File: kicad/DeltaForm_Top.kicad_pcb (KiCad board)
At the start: 2 copper layers, 85.4 x 128.6 mm, 21 parts

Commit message: added MCU
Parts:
- moved SPMP10 270.0 mm to (466.4, 132.9)
- moved SPMP11 270.0 mm to (485.4, 132.9)
- moved SPMP13 270.0 mm to (466.4, 151.9)
- moved SPMP14 270.0 mm to (485.4, 151.9)
- moved SPMP16 270.0 mm to (466.4, 171.0)
- moved SPMP17 270.0 mm to (485.4, 171.0)
- moved SPMP18 270.0 mm to (485.4, 190.0)
- moved SPMP3 270.0 mm to (466.4, 90.0)
- moved SPMP4 270.0 mm to (466.4, 113.8)
- moved SPMP5 270.0 mm to (485.4, 90.0)
- moved SPMP6 270.0 mm to (485.4, 113.8)
- moved SPMP1 270.0 mm to (447.3, 90.0)
- moved SPMP12 270.0 mm to (447.3, 151.9)
- moved SPMP15 270.0 mm to (447.3, 171.0)
- moved SPMP19 270.0 mm to (504.5, 142.4)
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
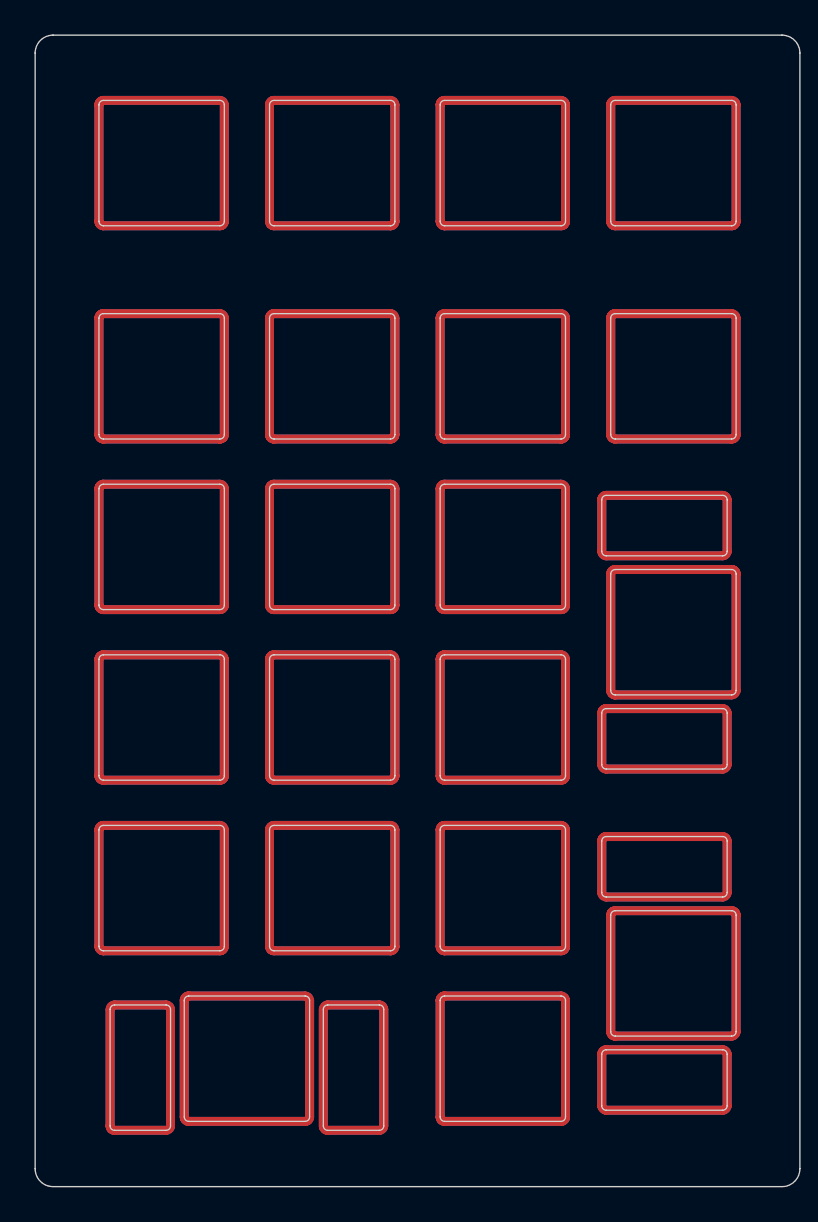
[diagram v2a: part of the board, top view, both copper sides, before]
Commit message: screw holes
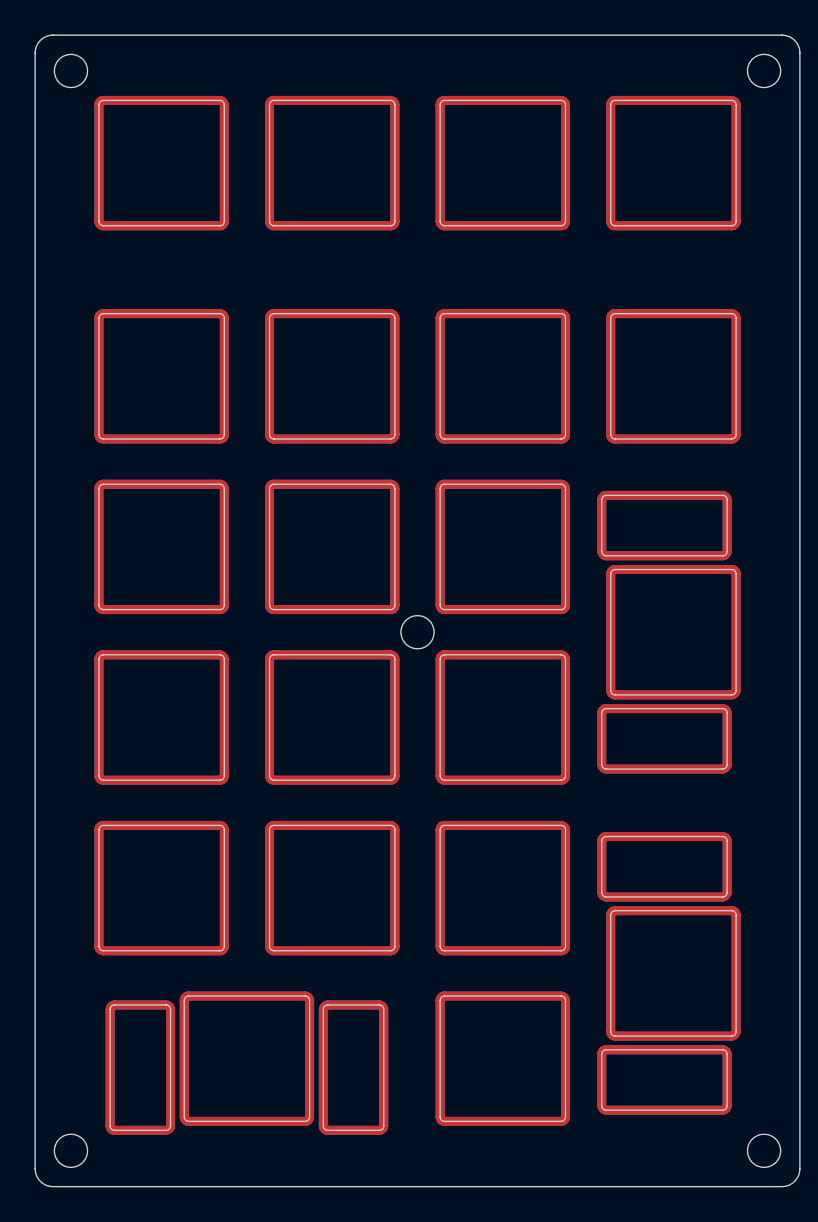
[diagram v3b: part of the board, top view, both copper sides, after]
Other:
- outline, holes or cut-outs redrawn
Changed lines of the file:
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@@
     (title "DeltaForm_Top")
     (date "2025-07-03")
-    (rev "0.3.4")
+    (rev "0.3.5")
     (company "Allen Choi")
   )
@@
 (gr_arc (start 516.575 204.3) (mid 517.9892136000001 203.71421360000002) (end 518.575 202.3) (layer Edge.Cuts) (stroke (width 0.15) (type default)))
 (gr_arc (start 433.17500000000007 202.3) (mid 433.7607864000001 203.71421360000002) (end 435.17500000000007 204.3) (layer Edge.Cuts) (stroke (width 0.15) (type default)))
+(gr_circle (center 437.17500000000007 79.7125) (end 439.0250000000001 79.7125) (layer Edge.Cuts) (stroke (width 0.15) (type default)) (fill none))
+(gr_circle (center 514.575 79.7125) (end 516.4250000000001 79.7125) (layer Edge.Cuts) (stroke (width 0.15) (type default)) (fill none))
+(gr_circle (center 514.575 200.30000000000004) (end 516.4250000000001 200.30000000000004) (layer Edge.Cuts) (stroke (width 0.15) (type default)) (fill none))
+(gr_circle (center 437.17500000000007 200.30000000000004) (end 439.0250000000001 200.30000000000004) (layer Edge.Cuts) (stroke (width 0.15) (type default)) (fill none))
+(gr_circle (center 475.87500000000006 142.38750000000002) (end 477.7250000000001 142.38750000000002) (layer Edge.Cuts) (stroke (width 0.15) (type default)) (fill none))
 )

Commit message: pogo pin - ergogen
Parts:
- moved SPMP10 270.0 mm to (196.3, 132.9)
- moved SPMP11 270.0 mm to (215.4, 132.9)
- moved SPMP13 270.0 mm to (196.3, 151.9)
- moved SPMP14 270.0 mm to (215.4, 151.9)
- moved SPMP16 270.0 mm to (196.3, 171.0)
- moved SPMP17 270.0 mm to (215.4, 171.0)
- moved SPMP18 270.0 mm to (215.4, 190.0)
- moved SPMP3 270.0 mm to (196.3, 90.0)
- moved SPMP4 270.0 mm to (196.3, 113.8)
- moved SPMP5 270.0 mm to (215.4, 90.0)
- moved SPMP6 270.0 mm to (215.4, 113.8)
- moved SPMP1 270.0 mm to (177.3, 90.0)
- moved SPMP12 270.0 mm to (177.3, 151.9)
- moved SPMP15 270.0 mm to (177.3, 171.0)
- moved SPMP19 270.0 mm to (234.4, 142.4)
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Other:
- outline, holes or cut-outs redrawn

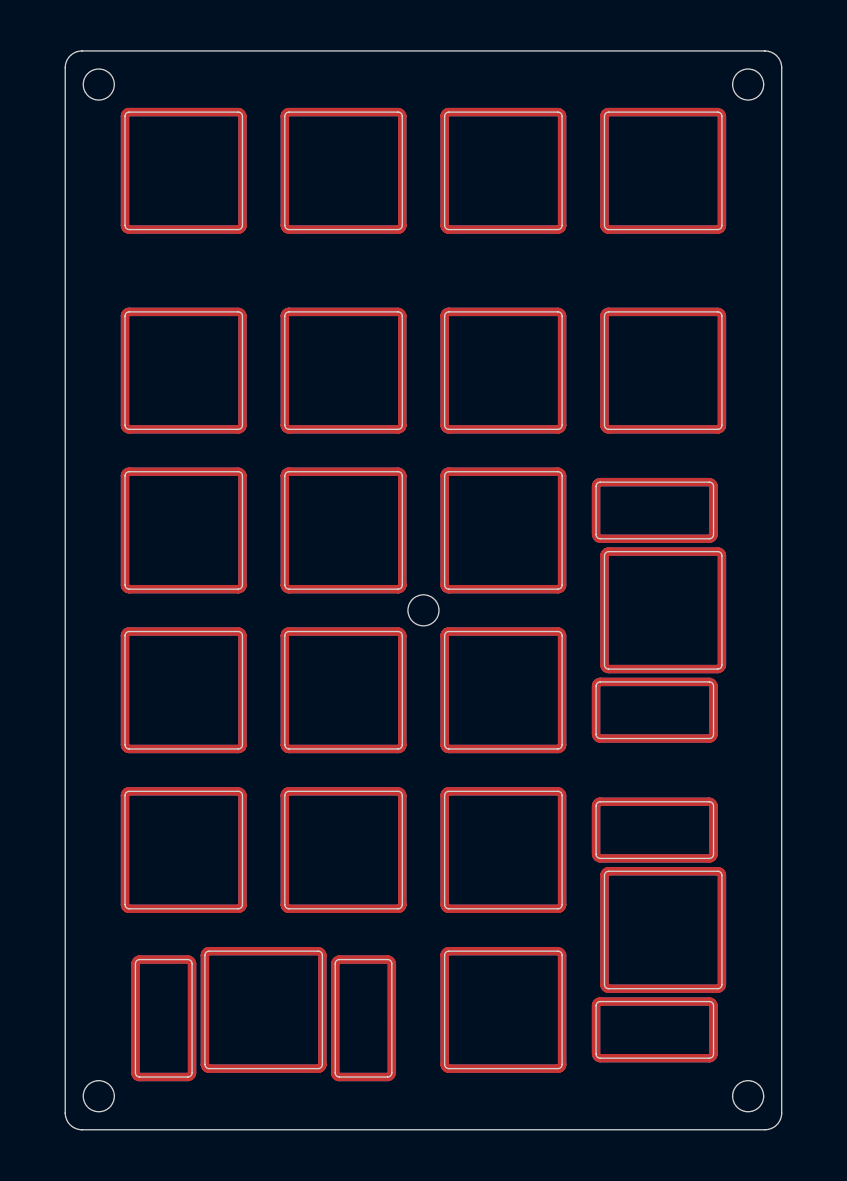
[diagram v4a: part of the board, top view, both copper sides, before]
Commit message: changed screw sizes
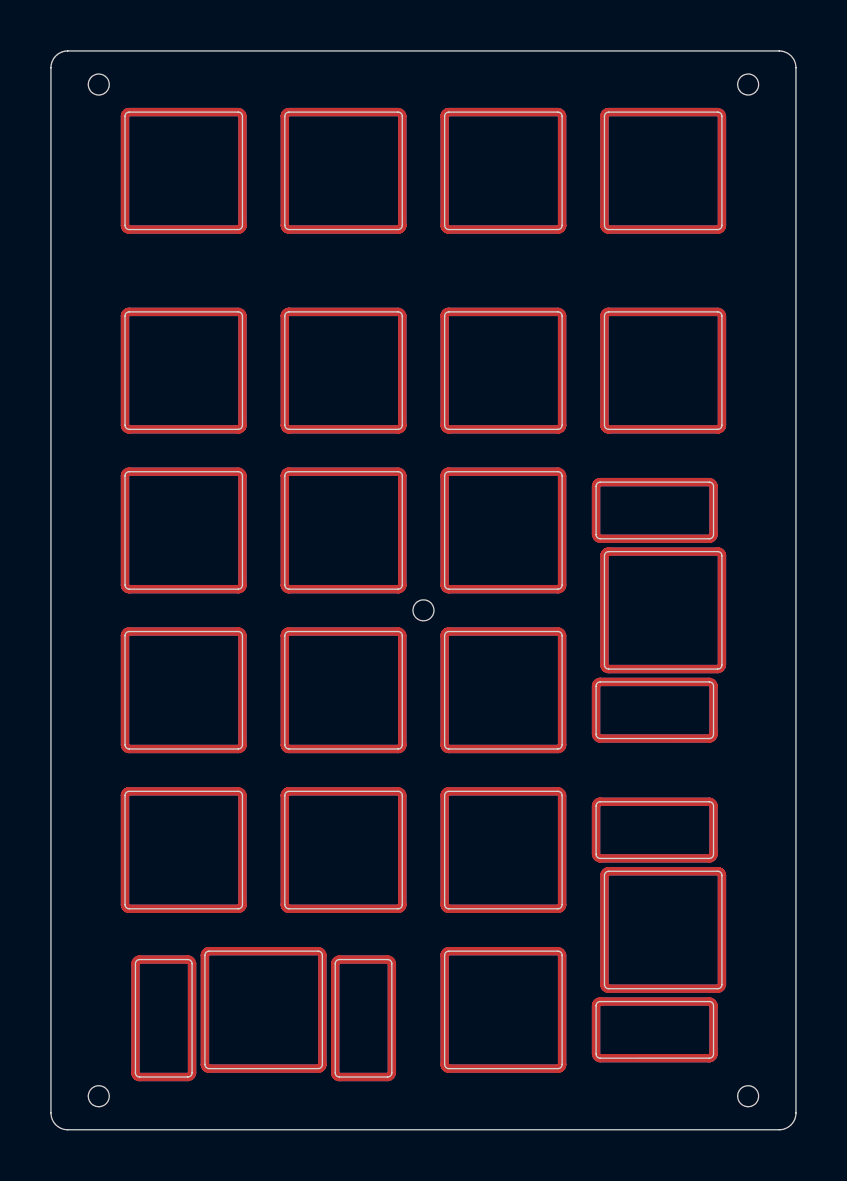
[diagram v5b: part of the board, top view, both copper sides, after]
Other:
- board size 85.4 x 128.6 mm -> 88.8 x 128.6 mm

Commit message: fixed positions for screw holes
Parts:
- moved SPMP10 270.0 mm to (466.4, 132.9)
- moved SPMP11 270.0 mm to (485.4, 132.9)
- moved SPMP13 270.0 mm to (466.4, 151.9)
- moved SPMP14 270.0 mm to (485.4, 151.9)
- moved SPMP16 270.0 mm to (466.4, 171.0)
- moved SPMP17 270.0 mm to (485.4, 171.0)
- moved SPMP18 270.0 mm to (485.4, 190.0)
- moved SPMP3 270.0 mm to (466.4, 90.0)
- moved SPMP4 270.0 mm to (466.4, 113.8)
- moved SPMP5 270.0 mm to (485.4, 90.0)
- moved SPMP6 270.0 mm to (485.4, 113.8)
- moved SPMP1 270.0 mm to (447.3, 90.0)
- moved SPMP12 270.0 mm to (447.3, 151.9)
- moved SPMP15 270.0 mm to (447.3, 171.0)
- moved SPMP19 270.0 mm to (504.5, 142.4)
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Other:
- outline, holes or cut-outs redrawn

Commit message: more tweaks  (#3)
* small tweaks

* GlyphMatrix - 3mm screws

* PhaseShift - 3mm screws

* DeltaForm - 3mm screws

* updated README.md
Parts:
- moved SPMP10 270.0 mm to (196.3, 132.9)
- moved SPMP11 270.0 mm to (215.4, 132.9)
- moved SPMP13 270.0 mm to (196.3, 151.9)
- moved SPMP14 270.0 mm to (215.4, 151.9)
- moved SPMP16 270.0 mm to (196.3, 171.0)
- moved SPMP17 270.0 mm to (215.4, 171.0)
- moved SPMP18 270.0 mm to (215.4, 190.0)
- moved SPMP3 270.0 mm to (196.3, 90.0)
- moved SPMP4 270.0 mm to (196.3, 113.8)
- moved SPMP5 270.0 mm to (215.4, 90.0)
- moved SPMP6 270.0 mm to (215.4, 113.8)
- moved SPMP1 270.0 mm to (177.3, 90.0)
- moved SPMP12 270.0 mm to (177.3, 151.9)
- moved SPMP15 270.0 mm to (177.3, 171.0)
- moved SPMP19 270.0 mm to (234.4, 142.4)
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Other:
- outline, holes or cut-outs redrawn

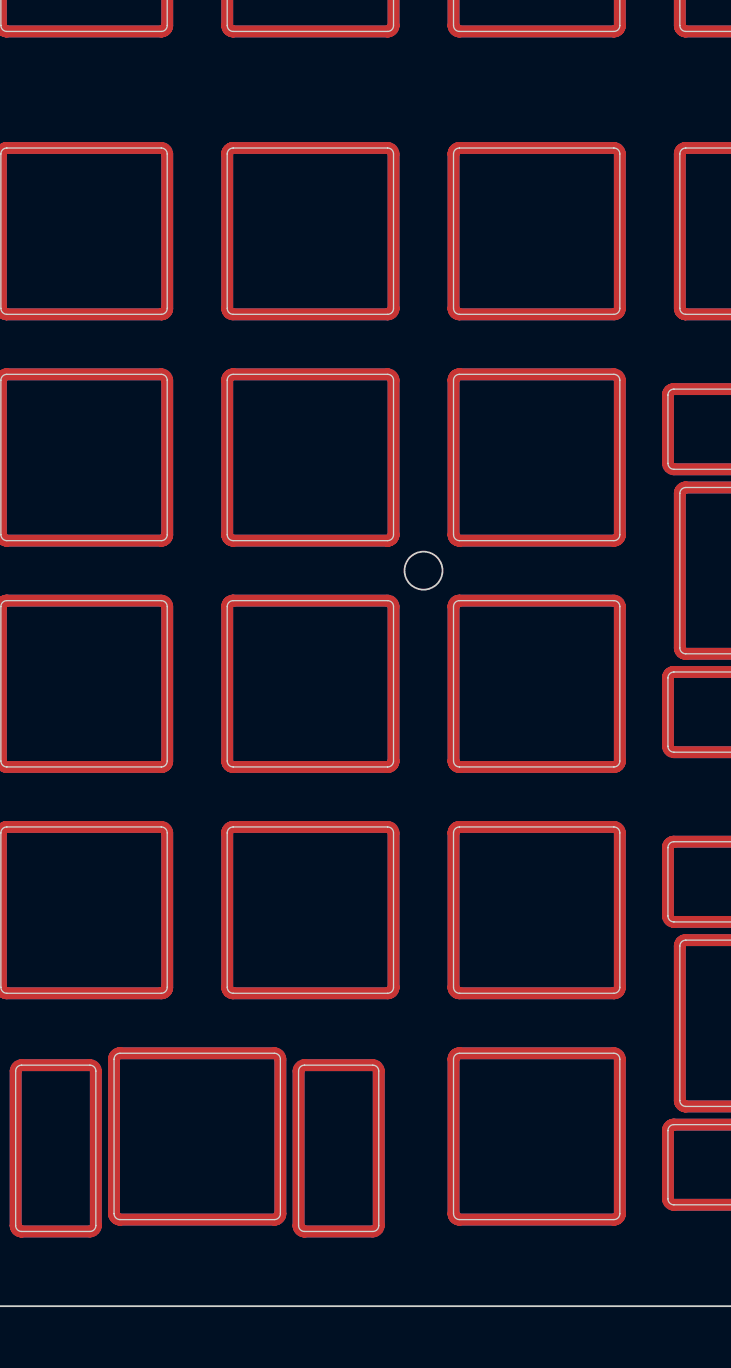
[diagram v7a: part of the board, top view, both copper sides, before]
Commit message: plates (#4)
* Silk Screen

* small changes for GlyphMatrix

* Silk screen for plates

* amended GlyphMatrix
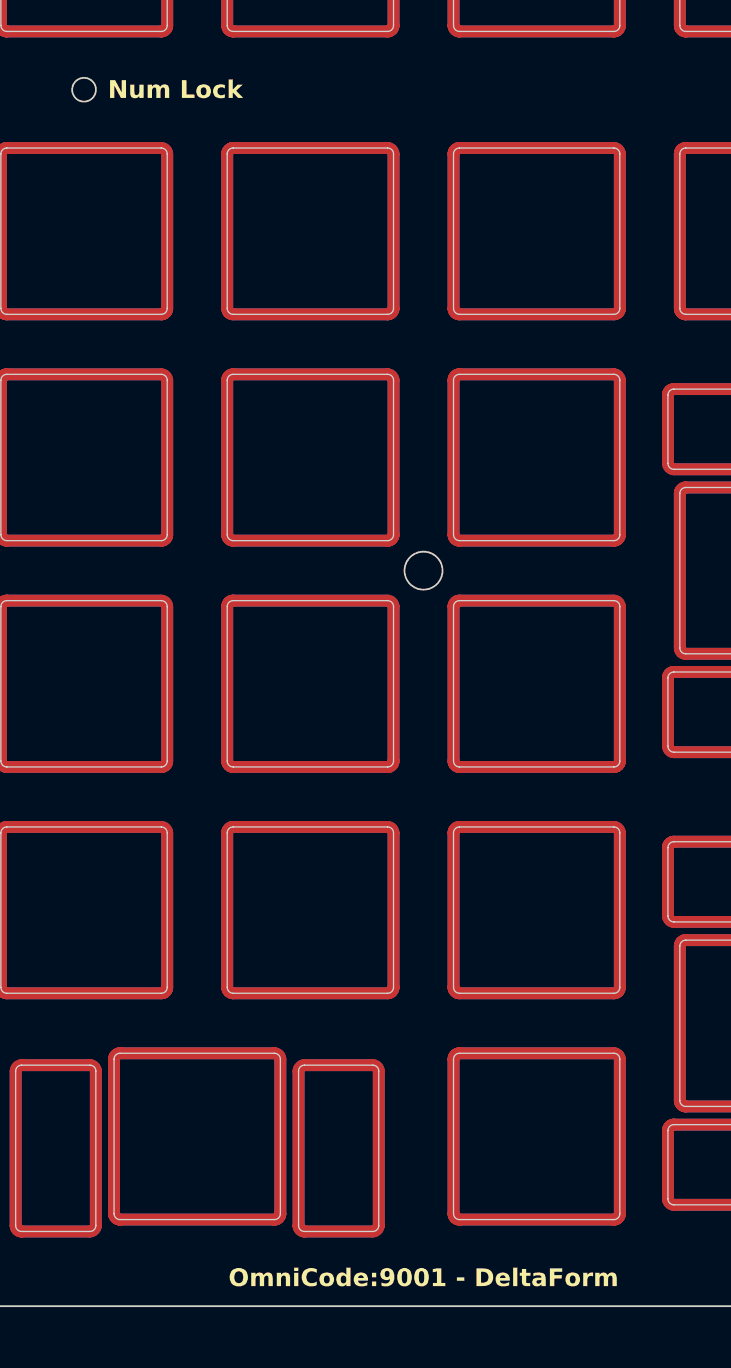
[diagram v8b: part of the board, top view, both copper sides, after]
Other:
- outline, holes or cut-outs redrawn
- board text added: "Num Lock"
- board text added: "OmniCode:9001 - DeltaForm"
